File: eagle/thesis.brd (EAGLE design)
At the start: 99.1 x 60.2 mm, 26 parts, among them U1 ITG-3200, U2 ADXL362, U3 MAX232PTH

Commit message: modified eagle boards and ordered.
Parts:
- added Q1, Q3: BSS138, SparkFun-DiscreteSemi:SOT23
- added R10, R11, R5, R6, R7, R9: 10K, rcl:R0603
- added R12, R8: 20K, rcl:R0603
- R3: value (none) -> 1K
- moved R3 3.69 mm to (23.0, 14.5)
- moved C10 2.79 mm to (31.2, 31.2)
- moved C11 2.50 mm to (29.6, 27.1)
- moved C8 2.43 mm to (31.4, 35.3)
- moved JP1 0.89 mm to (26.0, 10.3), turned to 0 degrees
- moved C9 0.64 mm to (31.1, 39.2)
- moved R4 0.63 mm to (31.4, 16.0)
- moved X1 0.38 mm to (7.37, 43.4), turned to 270 degrees
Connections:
- removed net SCL: HMC5883L.1, R2.1, U$1.SCL
- removed net SDA: HMC5883L.16, R1.1, U$1.SDA
- new net RX2H: R11.2, U$6.TTLDO
- new net RX3H: R7.2, U$3.P$5
- new net TX2H: Q1.3, R10.1, U$6.TTLDI
- new net TX3H: Q3.3, R6.1, U$3.P$2
- net 3V3: now also Q1.1, Q3.1, R5.2, R9.2
- net 5V: now also R10.2, R6.2, U$3.P$3
- net GND: now also R12.1, R8.1, U$3.P$6; no longer U1.12
- net RX2: now also R11.1, R12.2; no longer U$6.TTLDO
- net RX3: now also R7.1, R8.2
- net SCL1: now also HMC5883L.1, R2.1, U$1.SCL
- net SDA1: now also HMC5883L.16, R1.1, U$1.SDA
- net TX2: now also Q1.2, R9.1; no longer U$6.TTLDI
- net TX3: now also Q3.2, R5.1
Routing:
- net GND: track 0.00 -> 377.7 mm, vias 0 -> 6
- net 3V3: track 0.00 -> 189.2 mm, vias 0 -> 6
- net 5V: track 0.00 -> 138.7 mm, vias 0 -> 3
- net D41: track 0.00 -> 131.2 mm
- net D44: track 0.00 -> 111.2 mm
- net D43: track 0.00 -> 110.1 mm
- net SCL1: track 0.00 -> 102.9 mm, vias 0 -> 2
- net TX1: track 0.00 -> 99.4 mm
- net D45: track 0.00 -> 99.4 mm
- net D39: track 0.00 -> 88.2 mm, vias 0 -> 1
- net D40: track 0.00 -> 88.0 mm
- net D42: track 0.00 -> 87.7 mm
- net RX3: track 0.00 -> 86.1 mm, vias 0 -> 1
- net TX3: track 0.00 -> 83.4 mm, vias 0 -> 2
- net RX1: track 0.00 -> 82.7 mm
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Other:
- board text added: "ADAM CHASE 10/22/13 FDR v3.00"
- board text added: "BSS138"
- board text added: "RS232SI"
- board text added: "RS232SO"
- board text added: "RX3H"
- board text added: "TX3H"
- board text added: "VIN"
- board text removed: "0.1uF"
- board text removed: "0.22uF"
- board text removed: "10nF"
- board text removed: "2.2nF"
- board text removed: "4.7K"
- board text removed: "4.7uF"
- board text removed: "ADAM CHASE 09/10/13 FDR v2.10"

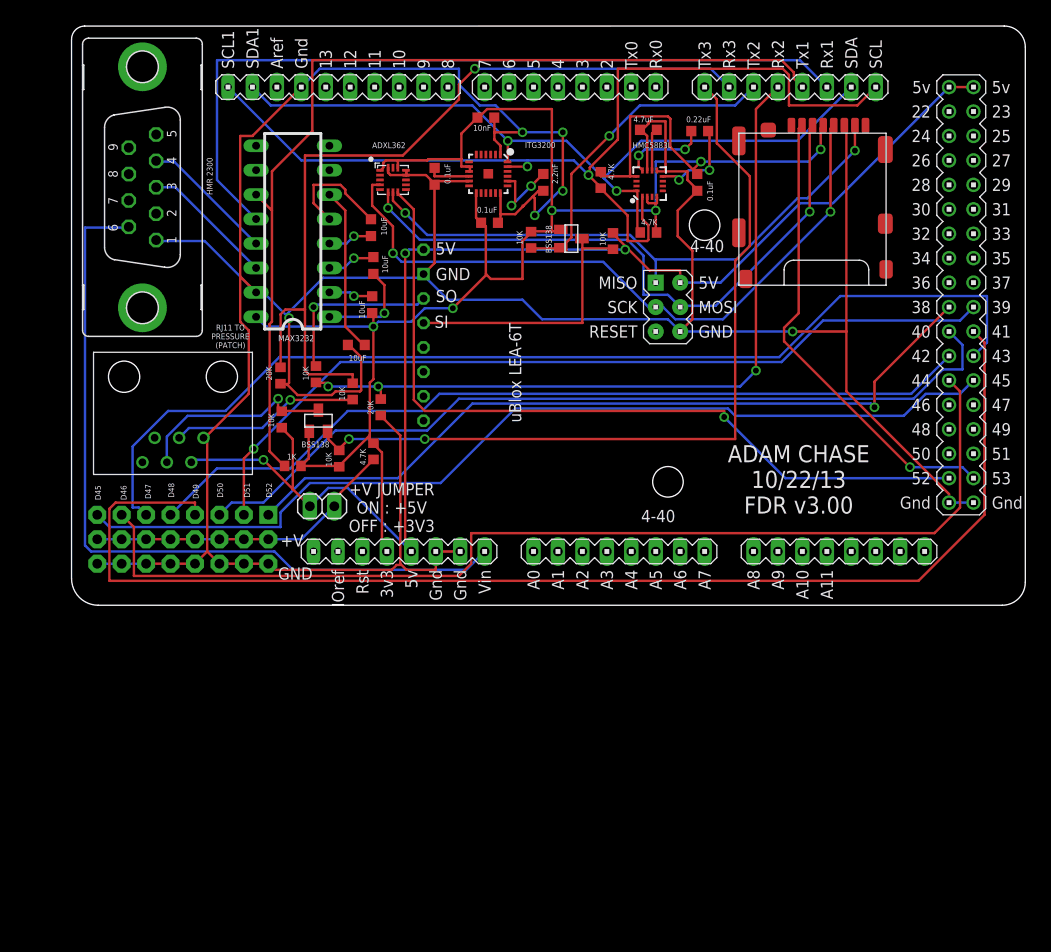
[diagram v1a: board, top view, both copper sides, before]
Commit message: modified gps board pad drill size and made thesis board a BOB.
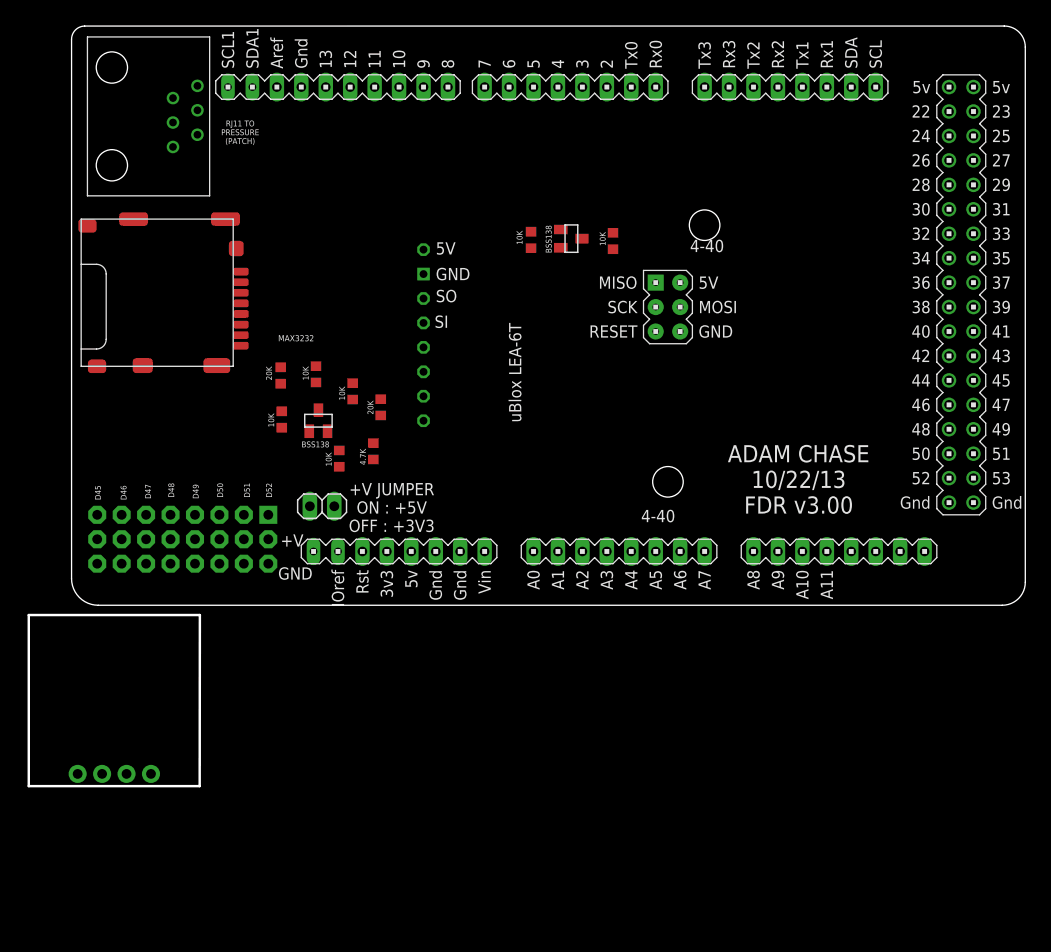
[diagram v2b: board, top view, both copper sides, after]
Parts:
- removed C1, C4, C6: 0.1uF, rcl:C0603K
- removed C10, C11, C8, C9: 10uF, rcl:C0603K
- removed C2: 2.2nF, rcl:C0603K
- removed C3: 4.7uF, rcl:C0603K
- removed C5: 0.22uF, rcl:C0603K
- removed C7: 10nF, rcl:C0603K
- removed HMC5883L: SPARKFUN_HMC5883LSMD, HMC5883L_Breakout-v11:SPARKFUN_16LPCC
- removed R1, R2: 4.7K, rcl:R0603
- removed R3: 1K, rcl:R0603
- removed U1: ITG-3200, SparkFun:QFN-24
- removed U2: ADXL362, SparkFun-Sensors:ADXL362
- removed U3: MAX232PTH, SparkFun-DigitalIC:DIL16
- removed X1: (no value), con-subd:F09VP
- added U$4: HMC5883L, HMC5883L:HMC5883L
- moved U$2 68.0 mm to (9.40, 32.6), turned to 270 degrees
- moved U$3 31.4 mm to (14.4, 42.5), turned to 90 degrees
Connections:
- removed net CPOUT: C2.2, U1.20
- removed net N$1: C10.2, U3.2
- removed net N$12: C3.1, HMC5883L.10
- removed net N$14: C1.2, U1.10
- removed net N$2: C11.2, U3.6
- removed net N$3: C9.1, U3.4
- removed net N$4: C9.2, U3.5
- removed net N$5: C5.1, HMC5883L.8
- removed net N$6: C8.1, U3.1
- removed net N$7: C5.2, HMC5883L.12
- removed net N$8: C8.2, U3.3
- removed net RS232SI: U3.14, X1.3
- removed net RS232SO: U3.13, X1.4
- net 3V3: no longer C10.1, C4.1, C6.2, C7.2, HMC5883L.13, HMC5883L.2, HMC5883L.4, R1.2, R2.2, R3.1, U1.13, U1.8, U1.9, U2.P$1, U2.P$14, U3.16
- net D52: no longer U2.P$8
- net GND: no longer C1.1, C11.1, C2.1, C3.2, C4.2, C6.1, C7.1, HMC5883L.11, HMC5883L.9, U1.1, U1.11, U1.18, U2.P$12, U2.P$13, U2.P$16, U3.15, X1.1
- net MISO: no longer U2.P$7
- net MOSI: no longer U2.P$6
- net RX1: no longer U3.12
- net SCL1: no longer HMC5883L.1, R2.1, U1.23
- net SCLK: no longer U2.P$4
- net SDA1: no longer HMC5883L.16, R1.1, U1.24
- net TX1: no longer R3.2, U3.11
- net VIN: no longer X1.6
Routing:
- net GND: track 377.7 -> 0.00 mm, vias 6 -> 0
- net 3V3: track 189.2 -> 0.00 mm, vias 6 -> 0
- net 5V: track 138.7 -> 0.00 mm, vias 3 -> 0
- net D41: track 131.2 -> 0.00 mm
- net D44: track 111.2 -> 0.00 mm
- net D43: track 110.1 -> 0.00 mm
- net SCL1: track 102.9 -> 0.00 mm, vias 2 -> 0
- net TX1: track 99.4 -> 0.00 mm
- net D45: track 99.4 -> 0.00 mm
- net D39: track 88.2 -> 0.00 mm, vias 1 -> 0
- net D40: track 88.0 -> 0.00 mm
- net D42: track 87.7 -> 0.00 mm
- net RX3: track 86.1 -> 0.00 mm, vias 1 -> 0
- net TX3: track 83.4 -> 0.00 mm, vias 2 -> 0
- net RX1: track 82.7 -> 0.00 mm
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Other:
- board text removed: "ADXL362"
- board text removed: "HMC5883L"
- board text removed: "HMR 2300"
- board text removed: "ITG3200"
- board text removed: "RS232SI"
- board text removed: "RS232SO"
- board text removed: "RX3H"
- board text removed: "TX3H"
- board text removed: "VIN"

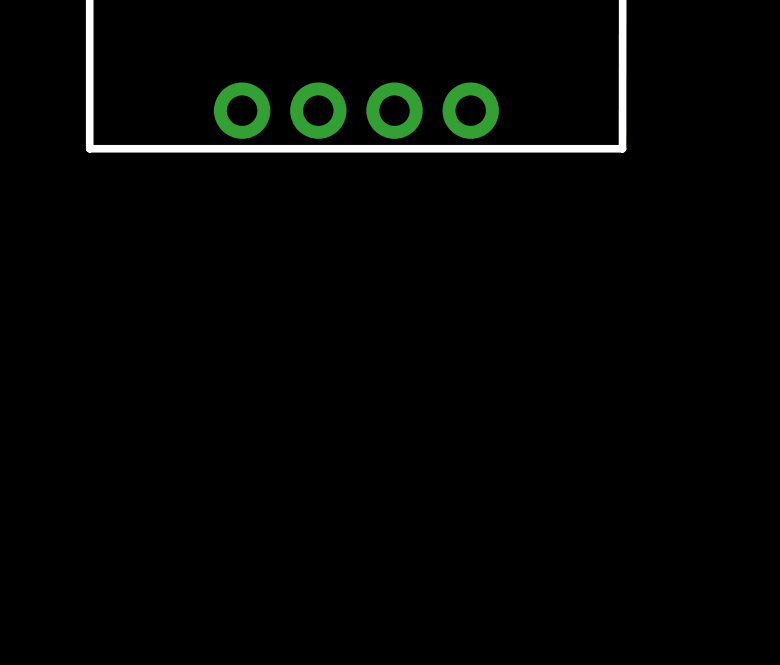
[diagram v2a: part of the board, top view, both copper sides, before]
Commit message: added itg3200
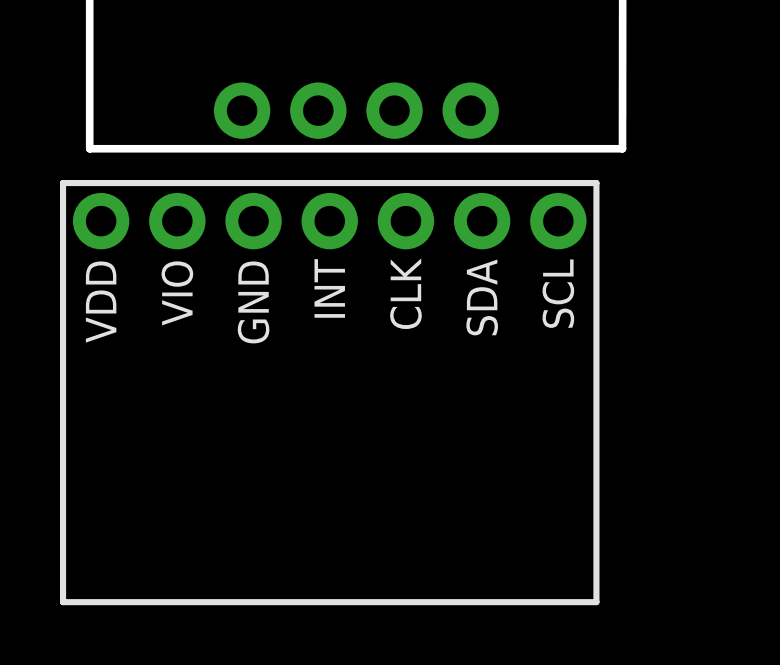
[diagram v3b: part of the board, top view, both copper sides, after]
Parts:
- added U$7: ITG3200, ITG3200:ITG3200
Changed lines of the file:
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@@
 </element>
 <element name="U$4" library="HMC5883L" package="HMC5883L" value="HMC5883L" x="-4.445" y="-18.796"/>
+<element name="U$7" library="ITG3200" package="ITG3200" value="ITG3200" x="-5.334" y="-33.909"/>
 </elements>
 <signals>
